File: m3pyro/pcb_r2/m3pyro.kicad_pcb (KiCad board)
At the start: 2 copper layers, 39 x 39 mm, 68 parts, among them IC1 STM32F405RxTx, IC2 TPS62130, IC3 MCP2562, IC4 TPS62150, J1 WEST TOP, J2 WEST BOT, J3 EAST TOP, J4 EAST BOT, Q1 Si5515CDC, Q2 Si5515CDC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

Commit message: m3pyro r2 routing progress
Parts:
- removed R1, R6: 10k, agg:0402
- moved D4 29.2 mm to (108.2, 108.2), turned to 270 degrees
- moved D5 28.0 mm to (106.3, 108.2), turned to 270 degrees
- moved Q4 24.8 mm to (95.5, 74.8)
- moved R22 24.8 mm to (96.6, 73.0)
- moved R26 24.8 mm to (94.5, 73.0)
- moved Q8 24.8 mm to (91.3, 74.8)
- moved R28 24.8 mm to (90.3, 73.0)
- moved R24 24.8 mm to (92.4, 73.0)
- moved Q7 23.8 mm to (101.3, 74.8)
- moved R14 23.8 mm to (102.4, 73.0)
- moved R18 23.8 mm to (100.3, 73.0)
- moved Q2 23.8 mm to (95.5, 69.8)
- moved R21 23.8 mm to (96.6, 68.0)
- moved R25 23.8 mm to (94.5, 68.0)
- moved Q3 23.8 mm to (105.5, 74.8)
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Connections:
- IC1 pad 20: Net-(IC1-Pad20) -> /SI_DIV
- IC1 pad 21: Net-(IC1-Pad21) -> /BUS_DIV
- IC1 pad 22: Net-(IC1-Pad22) -> /CONT
- IC1 pad 23: Net-(IC1-Pad23) -> /CONT_EN
- IC1 pad 30: Net-(IC1-Pad30) -> /CH3
- IC1 pad 33: Net-(IC1-Pad33) -> /CH7
- IC1 pad 34: Net-(IC1-Pad34) -> /CH1
- IC1 pad 35: Net-(IC1-Pad35) -> /CH5
- IC1 pad 36: Net-(IC1-Pad36) -> /CH2
- IC1 pad 37: Net-(IC1-Pad37) -> /CH6
- IC1 pad 38: Net-(IC1-Pad38) -> /CH4
- IC1 pad 39: Net-(IC1-Pad39) -> /CH8
- IC1 pad 40: Net-(IC1-Pad40) -> /CONT_EN
- IC1 pad 41: Net-(IC1-Pad41) -> /CONT
- IC1 pad 42: Net-(IC1-Pad42) -> /BUS_DIV
- IC1 pad 43: Net-(IC1-Pad43) -> /1A_EN
- IC1 pad 44: Net-(IC1-Pad44) -> /SI_DIV
- IC1 pad 45: Net-(IC1-Pad45) -> /3A_EN
- IC1 pad 59: Net-(IC1-Pad59) -> 3v3
- IC2 pad 5: Net-(IC2-Pad5) -> GND
- IC4 pad 5: Net-(IC4-Pad5) -> GND
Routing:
- net GND: track 0.00 -> 91.9 mm, vias 0 -> 31
- net 3v3: track 0.00 -> 82.3 mm, vias 0 -> 3
- net /PYRO_SI: track 0.00 -> 73.5 mm, vias 0 -> 9
- net /3A_EN: track 0.00 -> 44.3 mm
- net /BUS_DIV: track 0.00 -> 43.7 mm
- net /BUS: track 0.00 -> 42.8 mm
- net /SI_DIV: track 0.00 -> 39.2 mm
- net /CONT_EN: track 0.00 -> 34.6 mm, vias 0 -> 2
- net /CONT: track 0.00 -> 32.5 mm
- net /1A_EN: track 0.00 -> 26.7 mm
- net /JTMS: track 0.00 -> 18.8 mm, vias 0 -> 2
- net /5v_CAN: track 0.00 -> 18.6 mm, vias 0 -> 4
- net /JTDO: track 0.00 -> 14.3 mm
- net /JTCK: track 0.00 -> 13.9 mm, vias 0 -> 1
- net /JTDI: track 0.00 -> 12.0 mm, vias 0 -> 1
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- added copper zone on B.Cu, net GND
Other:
- net class Default: via_dia 0.8 -> 0.6; via_drill 0.4 -> 0.3

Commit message: further m3pyro r2 routing
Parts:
- moved Q2 4.81 mm to (99.0, 73.2)
- moved Q6 4.81 mm to (94.8, 73.2)
- moved R21 4.81 mm to (100.0, 71.3)
- moved R25 4.81 mm to (97.9, 71.3)
- moved R27 4.81 mm to (93.7, 71.3)
- moved R23 4.81 mm to (95.8, 71.3)
- moved Q4 4.34 mm to (99.0, 77.5)
- moved Q8 4.34 mm to (94.8, 77.5)
- moved R22 4.34 mm to (100.0, 75.7)
- moved R26 4.34 mm to (97.9, 75.7)
- moved R28 4.34 mm to (93.7, 75.7)
- moved R24 4.34 mm to (95.8, 75.7)
- moved Q5 3.85 mm to (103.2, 73.2)
- moved Q1 3.85 mm to (107.3, 73.2)
- moved R11 3.85 mm to (108.4, 71.3)
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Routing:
- net /SI_DIV: track 39.2 -> 41.0 mm
- net /3A_EN: track 44.3 -> 45.7 mm
- net /1A_EN: track 26.7 -> 28.0 mm
- net /BUS_DIV: track 43.7 -> 44.9 mm
- net /CONT: track 32.5 -> 33.5 mm
- net /CONT_EN: track 34.6 -> 35.5 mm
- net GND: track 91.9 -> 92.9 mm, vias 31 -> 30
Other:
- net class ThruInterconnect added: clearance 0.16, trace_width 0.25, via_dia 0.6, via_drill 0.3

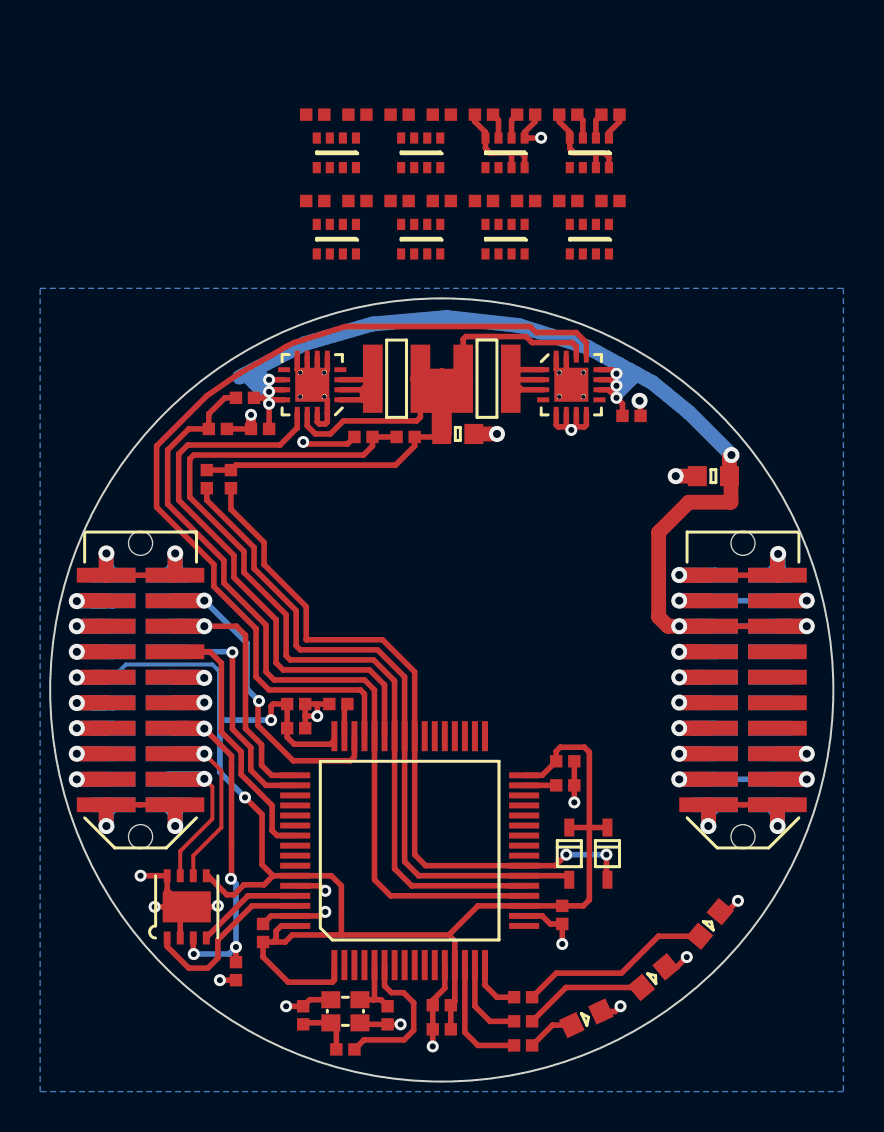
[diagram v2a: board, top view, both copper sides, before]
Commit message: fully routed m3pyro
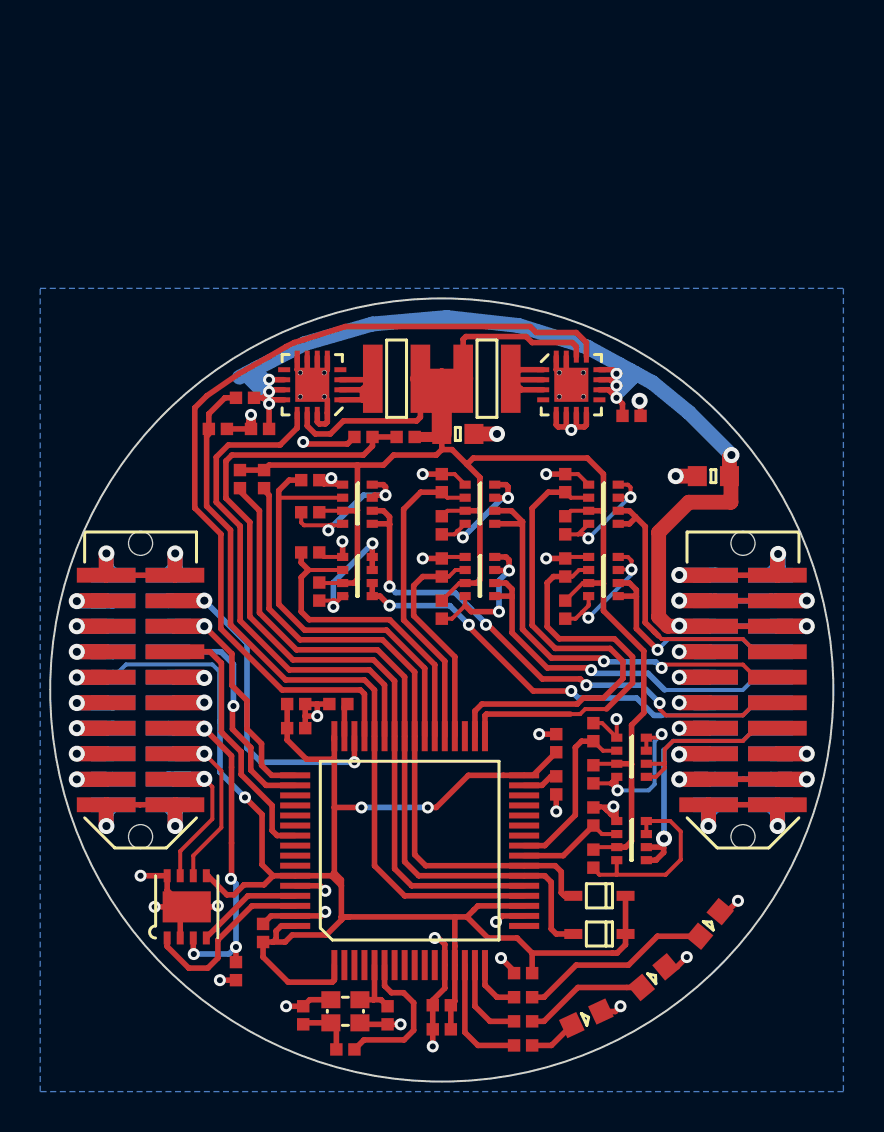
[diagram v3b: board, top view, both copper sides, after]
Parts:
- moved R28 35.6 mm to (107.5, 108.4), turned to 270 degrees
- moved Q8 33.4 mm to (109.5, 107.5), turned to 0 degrees
- moved R24 32.8 mm to (107.5, 106.3), turned to 90 degrees
- moved R26 30.1 mm to (107.5, 104.2), turned to 270 degrees
- moved Q4 27.9 mm to (109.5, 103.3), turned to 0 degrees
- moved R22 27.5 mm to (107.5, 102.1), turned to 90 degrees
- moved R27 25.4 mm to (100.0, 96.0), turned to 270 degrees
- moved R17 25.1 mm to (93.9, 95.1), turned to 270 degrees
- moved R13 24.3 mm to (93.5, 93.2)
- moved R15 23.6 mm to (93.5, 91.2)
- moved R11 23.6 mm to (93.5, 89.5)
- moved R23 22.9 mm to (100.0, 93.9), turned to 90 degrees
- moved Q5 22.3 mm to (95.8, 94.3), turned to 0 degrees
- moved Q6 22.3 mm to (101.9, 94.3), turned to 0 degrees
- moved Q1 21.0 mm to (95.8, 90.8), turned to 0 degrees
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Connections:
- IC1 pad 24: Net-(IC1-Pad24) -> /CH8
- IC1 pad 25: Net-(IC1-Pad25) -> /CH4
- IC1 pad 30: /CH3 -> Net-(IC1-Pad30)
- IC1 pad 33: /CH7 -> /CH5
- IC1 pad 35: /CH5 -> Net-(IC1-Pad35)
- IC1 pad 36: /CH2 -> /CH6
- IC1 pad 37: /CH6 -> /CH2
- IC1 pad 38: /CH4 -> /CH7
- IC1 pad 39: /CH8 -> /CH3
- Q1 pad 2: /CH1 -> /CH3
- Q1 pad 5: /PYRO1 -> /PYRO3
- Q1 pad 6: /PYRO1 -> /PYRO3
- Q3 pad 2: /CH3 -> /CH1
- Q3 pad 5: /PYRO3 -> /PYRO1
- Q3 pad 6: /PYRO3 -> /PYRO1
- Q5 pad 2: /CH5 -> /CH7
- Q5 pad 5: /PYRO5 -> /PYRO7
- Q5 pad 6: /PYRO5 -> /PYRO7
- Q7 pad 2: /CH7 -> /CH5
- Q7 pad 5: /PYRO7 -> /PYRO5
- Q7 pad 6: /PYRO7 -> /PYRO5
- R11 pad 1: /CH1 -> /CH3
- R12 pad 1: /CH3 -> /CH1
- R13 pad 1: /CH5 -> /CH7
- R14 pad 1: /CH7 -> /CH5
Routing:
- net /BUS: track 42.8 -> 96.6 mm
- net /PYRO3: track 0.00 -> 27.8 mm, vias 0 -> 4
- net /PYRO7: track 0.00 -> 23.3 mm, vias 0 -> 3
- net /CH1: track 1.28 -> 24.5 mm
- net /PYRO2: track 0.00 -> 22.2 mm, vias 0 -> 2
- net /CH3: track 0.00 -> 22.2 mm
- net GND: track 92.9 -> 111.6 mm, vias 30 -> 40
- net /CH5: track 1.28 -> 19.7 mm
- net /PYRO6: track 0.00 -> 18.3 mm, vias 0 -> 1
- net /CH7: track 0.00 -> 16.3 mm
- net /CH2: track 0.00 -> 15.7 mm
- net /PYRO1: track 0.00 -> 14.7 mm
- net /PYRO8: track 0.00 -> 12.8 mm, vias 0 -> 1
- net 3v3: track 82.4 -> 95.1 mm, vias 3 -> 4
- net /PYRO5: track 0.00 -> 11.5 mm, vias 0 -> 1
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
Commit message: silk, tidyup, etc
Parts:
- added C17: 10µ, agg:0603, F.Cu at (86.7, 89.0)
- moved C12 2.02 mm to (112.3, 87.8), turned to 0 degrees
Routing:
- net /PYRO_SI: track 73.5 -> 79.4 mm, vias 9 -> 10
- net GND: track 111.6 -> 112.9 mm, vias 40 -> 41
- net /BUS: track 96.6 -> 97.9 mm
- added copper zone on F.Cu, net /PYRO_SI
- added copper zone on F.Cu, net Net-(IC2-Pad1)
- added copper zone on F.Cu, net Net-(IC4-Pad1)
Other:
- board text added: "1"
- board text added: "1A"
- board text added: "2"
- board text added: "3"
- board text added: "3A"
- board text added: "4"
- board text added: "5"
- board text added: "6"
- board text added: "7"
- board text added: "8"
- board text added: "M3PYRO"
- board text added: "r2 AG 20/7/17"

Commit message: LED labels, gerbers
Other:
- board text added: "ERR"
- board text added: "OK"
- board text added: "WARN"
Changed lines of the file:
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@@
   (general
     (thickness 1.6)
-    (drawings 13)
+    (drawings 16)
     (tracks 1130)
     (zones 0)
@@
     (visible_elements FFF9FF5F)
     (pcbplotparams
-      (layerselection 0x00030_ffffffff)
-      (usegerberextensions false)
+      (layerselection 0x010f0_ffffffff)
+      (usegerberextensions true)
       (excludeedgelayer true)
       (linewidth 0.100000)
@@
       (psnegative false)
       (psa4output false)
-      (plotreference true)
-      (plotvalue true)
+      (plotreference false)
+      (plotvalue false)
       (plotinvisibletext false)
       (padsonsilk false)
-      (subtractmaskfromsilk false)
+      (subtractmaskfromsilk true)
       (outputformat 1)
       (mirror false)
-      (drillshape 1)
+      (drillshape 0)
       (scaleselection 1)
-      (outputdirectory ""))
+      (outputdirectory gerbers/))
   )
   (net 0 "")
@@
       (net 2 GND))
   )
+  (gr_text ERR (at 106.6 115.1 25) (layer F.SilkS)
+    (effects (font (size 1 1) (thickness 0.25)))
+  )
+  (gr_text WARN (at 109.7 113.15 40) (layer F.SilkS)
+    (effects (font (size 1 1) (thickness 0.25)))
+  )
+  (gr_text OK (at 112.35 110.75 50) (layer F.SilkS)
+    (effects (font (size 1 1) (thickness 0.25)))
+  )
   (gr_text 1A (at 95.5 82.25) (layer F.SilkS)

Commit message: slight further tidyup of myp3yro
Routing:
- net Net-(Q8-Pad4): track 9.62 -> 12.7 mm

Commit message: Amend SMPS output cap on m3pyro r2 to 22u
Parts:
- C16: value 10µ -> 22µ
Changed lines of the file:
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@@
   )
   (setup
-    (last_trace_width 0.28)
+    (last_trace_width 0.25)
     (user_trace_width 0.2)
     (user_trace_width 0.28)
@@
       (effects (font (size 1 1) (thickness 0.15)))
     )
-    (fp_text value 10µ (at 2.225 0 90) (layer F.Fab)
-      (effects (font (size 1 1) (thickness 0.15)))
-    )
+    (fp_text value 22µ (at 2.225 0 90) (layer F.Fab)
+      (effects (font (size 1 1) (thickness 0.15)))
+    )

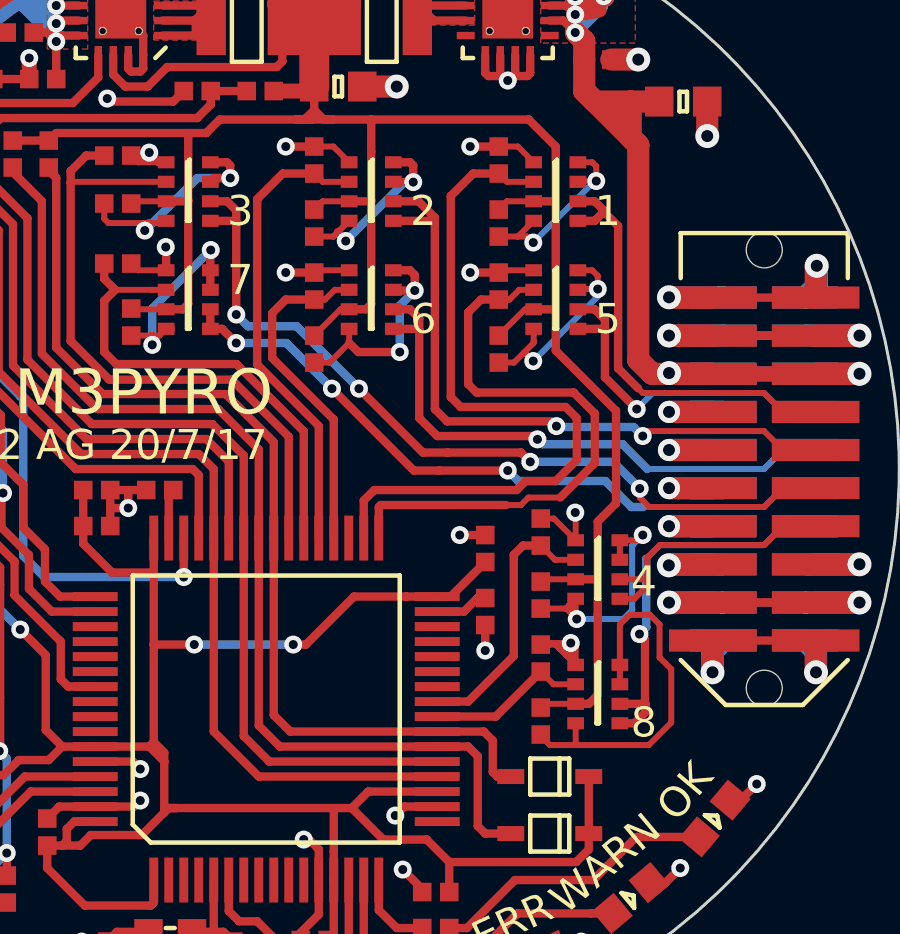
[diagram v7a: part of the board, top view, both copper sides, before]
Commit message: Update m3pyro so ch1-4 are bottom, 5-8 are top
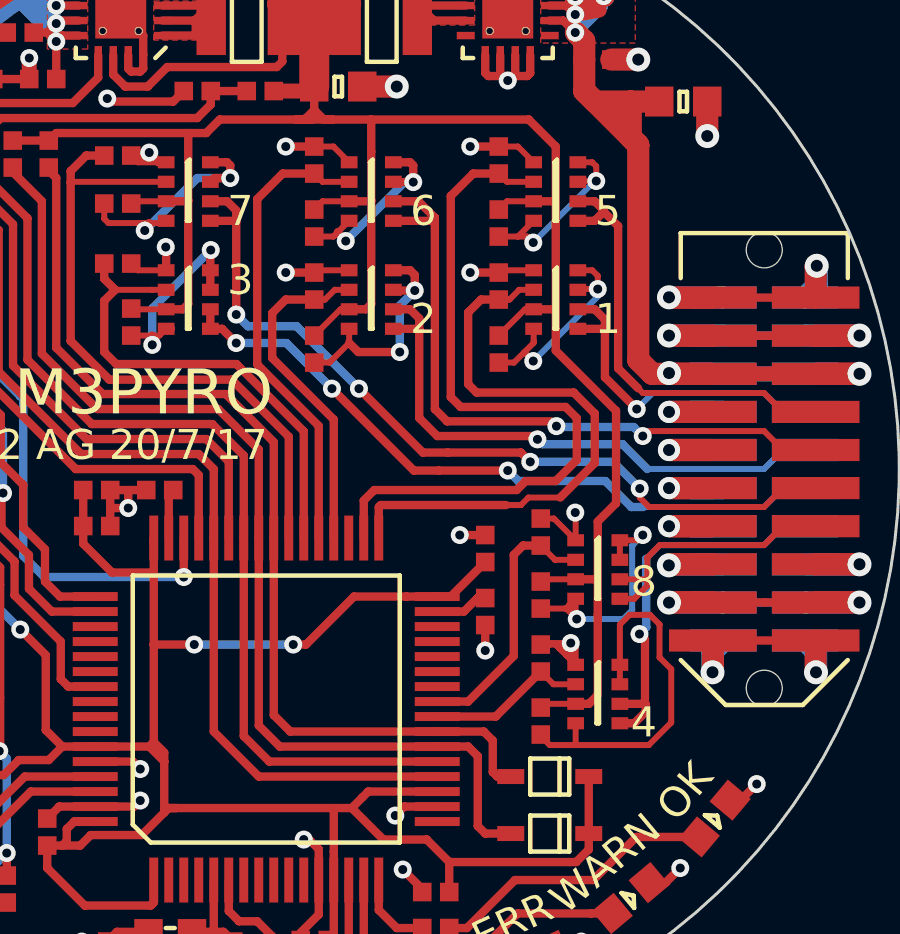
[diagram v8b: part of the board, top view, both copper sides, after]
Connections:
- IC1 pad 24: /CH8 -> /CH4
- IC1 pad 25: /CH4 -> /CH8
- IC1 pad 33: /CH5 -> /CH1
- IC1 pad 34: /CH1 -> /CH5
- IC1 pad 36: /CH6 -> /CH2
- IC1 pad 37: /CH2 -> /CH6
- IC1 pad 38: /CH7 -> /CH3
- IC1 pad 39: /CH3 -> /CH7
- J3 pad 10: /PYRO2 -> /PYRO6
- J3 pad 12: /PYRO3 -> /PYRO7
- J3 pad 14: /PYRO4 -> /PYRO8
- J3 pad 8: /PYRO1 -> /PYRO5
- J4 pad 10: /PYRO6 -> /PYRO2
- J4 pad 12: /PYRO7 -> /PYRO3
- J4 pad 14: /PYRO8 -> /PYRO4
- J4 pad 8: /PYRO5 -> /PYRO1
- Q1 pad 2: /CH3 -> /CH7
- Q1 pad 5: /PYRO3 -> /PYRO7
- Q1 pad 6: /PYRO3 -> /PYRO7
- Q2 pad 2: /CH2 -> /CH6
- Q2 pad 5: /PYRO2 -> /PYRO6
- Q2 pad 6: /PYRO2 -> /PYRO6
- Q3 pad 2: /CH1 -> /CH5
- Q3 pad 5: /PYRO1 -> /PYRO5
- Q3 pad 6: /PYRO1 -> /PYRO5
- Q4 pad 2: /CH4 -> /CH8
- Q4 pad 5: /PYRO4 -> /PYRO8
- Q4 pad 6: /PYRO4 -> /PYRO8
- Q5 pad 2: /CH7 -> /CH3
- Q5 pad 5: /PYRO7 -> /PYRO3
- Q5 pad 6: /PYRO7 -> /PYRO3
- Q6 pad 2: /CH6 -> /CH2
- Q6 pad 5: /PYRO6 -> /PYRO2
- Q6 pad 6: /PYRO6 -> /PYRO2
- Q7 pad 2: /CH5 -> /CH1
- Q7 pad 5: /PYRO5 -> /PYRO1
- Q7 pad 6: /PYRO5 -> /PYRO1
- Q8 pad 2: /CH8 -> /CH4
- Q8 pad 5: /PYRO8 -> /PYRO4
- Q8 pad 6: /PYRO8 -> /PYRO4
- R11 pad 1: /CH3 -> /CH7
- R12 pad 1: /CH1 -> /CH5
- R13 pad 1: /CH7 -> /CH3
- R14 pad 1: /CH5 -> /CH1
- R21 pad 1: /CH2 -> /CH6
- R22 pad 1: /CH4 -> /CH8
- R23 pad 1: /CH6 -> /CH2
- R24 pad 1: /CH8 -> /CH4
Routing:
- net /CH7: track 16.3 -> 22.2 mm
- net /CH3: track 22.2 -> 16.3 mm
- net /CH5: track 20.0 -> 24.7 mm
- net /CH1: track 24.7 -> 20.0 mm
- net /PYRO7: track 23.2 -> 27.7 mm, vias 3 -> 4
- net /PYRO3: track 27.7 -> 23.2 mm, vias 4 -> 3
- net /CH6: track 11.2 -> 15.7 mm
- net /CH2: track 15.7 -> 11.2 mm
- net /PYRO8: track 12.9 -> 9.08 mm, vias 1 -> 0
- net /PYRO4: track 9.08 -> 12.9 mm, vias 0 -> 1
- net /PYRO6: track 19.0 -> 22.8 mm, vias 1 -> 2
- net /PYRO2: track 22.8 -> 19.0 mm, vias 2 -> 1
- net /CH8: track 5.41 -> 8.94 mm
- net /CH4: track 8.94 -> 5.41 mm
- net /PYRO5: track 11.5 -> 14.6 mm, vias 1 -> 0
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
